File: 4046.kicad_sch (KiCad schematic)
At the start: 10 parts, among them SW2 PLL Type, U2 4046

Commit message: schematic finished
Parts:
- renumbered R6 to R10, R8 to R11, R4 to R8, R5 to R9, SW2 to SW6
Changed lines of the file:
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@@
+					(unit 1)
+				)
+				(path "/01c1f2c1-4d06-4880-847a-9ab55552e3fd/ad1f1d92-237d-4bc3-883c-2ce266dd223f/a3fe2060-ea4c-4d2b-9ba5-3084b7e4dd13"
+					(reference "C4")
 					(unit 1)
 				)
@@
 		(on_board yes)
 		(dnp no)
-		(property "Reference" "SW2"
+		(property "Reference" "SW6"
 			(at 179.07 65.024 0)
 			(effects
@@
 			(project "kleingorium"
 				(path "/01c1f2c1-4d06-4880-847a-9ab55552e3fd/ad1f1d92-237d-4bc3-883c-2ce266dd223f/24602293-d4e4-4f10-aa56-94ee1e111e94"
-					(reference "SW2")
+					(reference "SW6")
+					(unit 1)
+				)
+				(path "/01c1f2c1-4d06-4880-847a-9ab55552e3fd/ad1f1d92-237d-4bc3-883c-2ce266dd223f/a3fe2060-ea4c-4d2b-9ba5-3084b7e4dd13"
+					(reference "SW7")
 					(unit 1)
 				)
@@
 		(dnp no)
 		(fields_autoplaced yes)
-		(property "Reference" "#PWR010"
+		(property "Reference" "#PWR017"
 			(at 152.4 50.8 0)
 			(effects
@@
 			(project "kleingorium"
 				(path "/01c1f2c1-4d06-4880-847a-9ab55552e3fd/ad1f1d92-237d-4bc3-883c-2ce266dd223f/24602293-d4e4-4f10-aa56-94ee1e111e94"
-					(reference "#PWR010")
+					(reference "#PWR017")
+					(unit 1)
+				)
+				(path "/01c1f2c1-4d06-4880-847a-9ab55552e3fd/ad1f1d92-237d-4bc3-883c-2ce266dd223f/a3fe2060-ea4c-4d2b-9ba5-3084b7e4dd13"
+					(reference "#PWR048")
 					(unit 1)
 				)
@@
 					(unit 1)
 				)
+				(path "/01c1f2c1-4d06-4880-847a-9ab55552e3fd/ad1f1d92-237d-4bc3-883c-2ce266dd223f/a3fe2060-ea4c-4d2b-9ba5-3084b7e4dd13"
+					(reference "U8")
+					(unit 1)
+				)
 			)
 		)
@@
 		(dnp no)
 		(fields_autoplaced yes)
-		(property "Reference" "R8"
+		(property "Reference" "R11"
 			(at 184.15 77.4699 0)
 			(effects
@@
 			(project "kleingorium"
 				(path "/01c1f2c1-4d06-4880-847a-9ab55552e3fd/ad1f1d92-237d-4bc3-883c-2ce266dd223f/24602293-d4e4-4f10-aa56-94ee1e111e94"
-					(reference "R8")
+					(reference "R11")
+					(unit 1)
+				)
+				(path "/01c1f2c1-4d06-4880-847a-9ab55552e3fd/ad1f1d92-237d-4bc3-883c-2ce266dd223f/a3fe2060-ea4c-4d2b-9ba5-3084b7e4dd13"
+					(reference "R29")
 					(unit 1)
 				)
@@
 		(dnp no)
 		(fields_autoplaced yes)
-		(property "Reference" "#PWR07"
+		(property "Reference" "#PWR015"
 			(at 128.27 114.3 0)
 			(effects
@@
 			(project "kleingorium"
 				(path "/01c1f2c1-4d06-4880-847a-9ab55552e3fd/ad1f1d92-237d-4bc3-883c-2ce266dd223f/24602293-d4e4-4f10-aa56-94ee1e111e94"
-					(reference "#PWR07")
+					(reference "#PWR015")
+					(unit 1)
+				)
+				(path "/01c1f2c1-4d06-4880-847a-9ab55552e3fd/ad1f1d92-237d-4bc3-883c-2ce266dd223f/a3fe2060-ea4c-4d2b-9ba5-3084b7e4dd13"
+					(reference "#PWR046")
 					(unit 1)
 				)
@@
 		(on_board yes)
 		(dnp no)
-		(property "Reference" "R6"
+		(property "Reference" "R10"
 			(at 192.278 65.532 0)
 			(effects
@@
 			(project "kleingorium"
 				(path "/01c1f2c1-4d06-4880-847a-9ab55552e3fd/ad1f1d92-237d-4bc3-883c-2ce266dd223f/24602293-d4e4-4f10-aa56-94ee1e111e94"
-					(reference "R6")
+					(reference "R10")
+					(unit 1)
+				)
+				(path "/01c1f2c1-4d06-4880-847a-9ab55552e3fd/ad1f1d92-237d-4bc3-883c-2ce266dd223f/a3fe2060-ea4c-4d2b-9ba5-3084b7e4dd13"
+					(reference "R28")
 					(unit 1)
 				)
@@
 		(dnp no)
 		(fields_autoplaced yes)
-		(property "Reference" "#PWR015"
+		(property "Reference" "#PWR019"
 			(at 173.99 115.57 0)
 			(effects
@@
 			(project "kleingorium"
 				(path "/01c1f2c1-4d06-4880-847a-9ab55552e3fd/ad1f1d92-237d-4bc3-883c-2ce266dd223f/24602293-d4e4-4f10-aa56-94ee1e111e94"
-					(reference "#PWR015")
+					(reference "#PWR019")
+					(unit 1)
+				)
+				(path "/01c1f2c1-4d06-4880-847a-9ab55552e3fd/ad1f1d92-237d-4bc3-883c-2ce266dd223f/a3fe2060-ea4c-4d2b-9ba5-3084b7e4dd13"
+					(reference "#PWR050")
 					(unit 1)
 				)
@@
 		(dnp no)
 		(fields_autoplaced yes)
-		(property "Reference" "R4"
+		(property "Reference" "R8"
 			(at 130.81 97.7899 0)
 			(effects
@@
 			(project "kleingorium"
 				(path "/01c1f2c1-4d06-4880-847a-9ab55552e3fd/ad1f1d92-237d-4bc3-883c-2ce266dd223f/24602293-d4e4-4f10-aa56-94ee1e111e94"
-					(reference "R4")
+					(reference "R8")
+					(unit 1)
+				)
+				(path "/01c1f2c1-4d06-4880-847a-9ab55552e3fd/ad1f1d92-237d-4bc3-883c-2ce266dd223f/a3fe2060-ea4c-4d2b-9ba5-3084b7e4dd13"
+					(reference "R26")
 					(unit 1)
 				)
@@
 		(dnp no)
 		(fields_autoplaced yes)
-		(property "Reference" "#PWR014"
+		(property "Reference" "#PWR018"
 			(at 152.4 114.3 0)
 			(effects
@@
 			(project "kleingorium"
 				(path "/01c1f2c1-4d06-4880-847a-9ab55552e3fd/ad1f1d92-237d-4bc3-883c-2ce266dd223f/24602293-d4e4-4f10-aa56-94ee1e111e94"
-					(reference "#PWR014")
+					(reference "#PWR018")
+					(unit 1)
+				)
+				(path "/01c1f2c1-4d06-4880-847a-9ab55552e3fd/ad1f1d92-237d-4bc3-883c-2ce266dd223f/a3fe2060-ea4c-4d2b-9ba5-3084b7e4dd13"
+					(reference "#PWR049")
 					(unit 1)
 				)
@@
 		(dnp no)
 		(fields_autoplaced yes)
-		(property "Reference" "R5"
+		(property "Reference" "R9"
 			(at 142.24 97.7899 0)
 			(effects
@@
 			(project "kleingorium"
 				(path "/01c1f2c1-4d06-4880-847a-9ab55552e3fd/ad1f1d92-237d-4bc3-883c-2ce266dd223f/24602293-d4e4-4f10-aa56-94ee1e111e94"
-					(reference "R5")
+					(reference "R9")
+					(unit 1)
+				)
+				(path "/01c1f2c1-4d06-4880-847a-9ab55552e3fd/ad1f1d92-237d-4bc3-883c-2ce266dd223f/a3fe2060-ea4c-4d2b-9ba5-3084b7e4dd13"
+					(reference "R27")
 					(unit 1)
 				)
@@
 		(on_board yes)
 		(dnp no)
-		(property "Reference" "#PWR06"
+		(property "Reference" "#PWR014"
 			(at 116.84 87.63 0)
 			(effects
@@
 			(project "kleingorium"
 				(path "/01c1f2c1-4d06-4880-847a-9ab55552e3fd/ad1f1d92-237d-4bc3-883c-2ce266dd223f/24602293-d4e4-4f10-aa56-94ee1e111e94"
-					(reference "#PWR06")
+					(reference "#PWR014")
+					(unit 1)
+				)
+				(path "/01c1f2c1-4d06-4880-847a-9ab55552e3fd/ad1f1d92-237d-4bc3-883c-2ce266dd223f/a3fe2060-ea4c-4d2b-9ba5-3084b7e4dd13"
+					(reference "#PWR045")
 					(unit 1)
 				)
@@
 					(unit 1)
 				)
+				(path "/01c1f2c1-4d06-4880-847a-9ab55552e3fd/ad1f1d92-237d-4bc3-883c-2ce266dd223f/a3fe2060-ea4c-4d2b-9ba5-3084b7e4dd13"
+					(reference "C6")
+					(unit 1)
+				)
 			)
 		)
@@
 		(dnp no)
 		(fields_autoplaced yes)
-		(property "Reference" "#PWR09"
+		(property "Reference" "#PWR016"
 			(at 139.7 114.3 0)
 			(effects
@@
 			(project "kleingorium"
 				(path "/01c1f2c1-4d06-4880-847a-9ab55552e3fd/ad1f1d92-237d-4bc3-883c-2ce266dd223f/24602293-d4e4-4f10-aa56-94ee1e111e94"
-					(reference "#PWR09")
+					(reference "#PWR016")
+					(unit 1)
+				)
+				(path "/01c1f2c1-4d06-4880-847a-9ab55552e3fd/ad1f1d92-237d-4bc3-883c-2ce266dd223f/a3fe2060-ea4c-4d2b-9ba5-3084b7e4dd13"
+					(reference "#PWR047")
 					(unit 1)
 				)
@@
 					(unit 1)
 				)
+				(path "/01c1f2c1-4d06-4880-847a-9ab55552e3fd/ad1f1d92-237d-4bc3-883c-2ce266dd223f/a3fe2060-ea4c-4d2b-9ba5-3084b7e4dd13"
+					(reference "C5")
+					(unit 1)
+				)
 			)
 		)
@@
 					(unit 1)
 				)
+				(path "/01c1f2c1-4d06-4880-847a-9ab55552e3fd/ad1f1d92-237d-4bc3-883c-2ce266dd223f/a3fe2060-ea4c-4d2b-9ba5-3084b7e4dd13"
+					(reference "RV2")
+					(unit 1)
+				)

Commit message: wip symmetric layout
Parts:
- renumbered C1 to C4, C2 to C5, C3 to C6, R8 to R27, R9 to R28, R10 to R29, R11 to R30, RV1 to RV2, U2 to U9

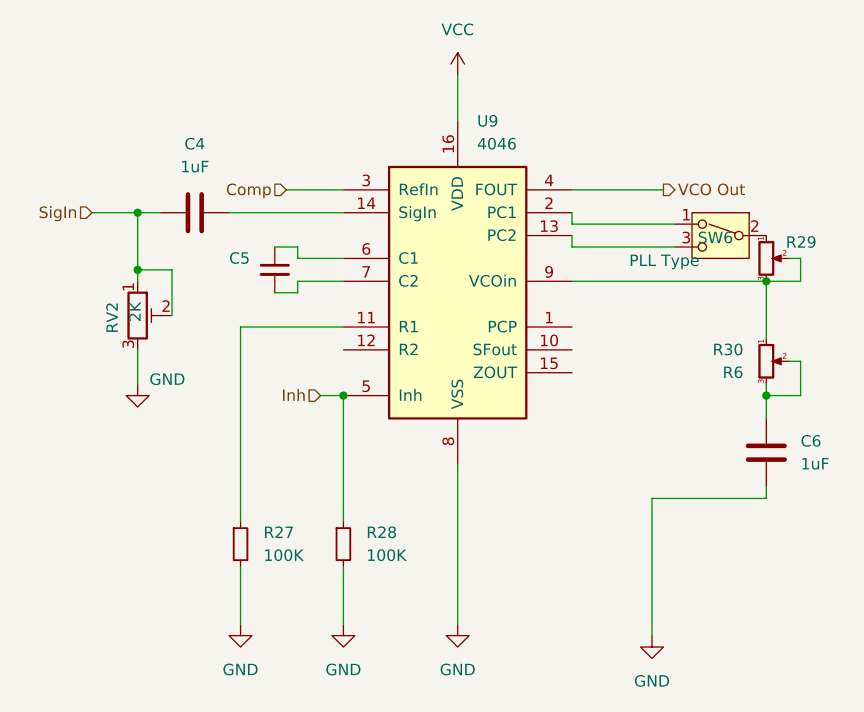
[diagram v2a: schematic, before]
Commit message: two halves routing
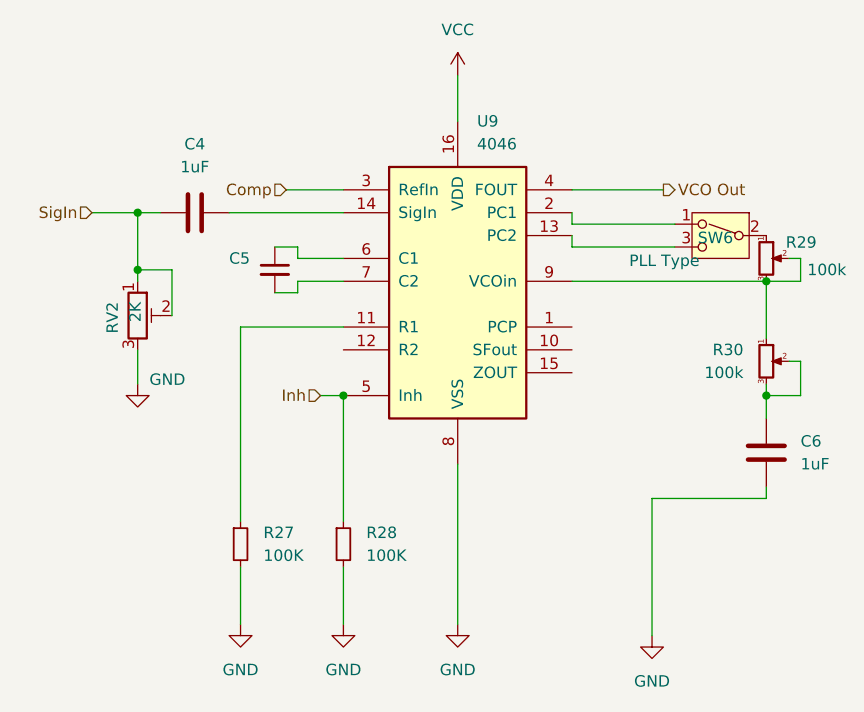
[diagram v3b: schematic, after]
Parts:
- R29: value R5 -> 100k
- R30: value R6 -> 100k
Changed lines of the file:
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@@
 			)
 		)
-		(property "Value" "R6"
+		(property "Value" "100k"
 			(at 184.15 80.0099 0)
 			(effects
@@
 			)
 		)
-		(property "Value" "R5"
-			(at 184.15 68.5799 0)
+		(property "Value" "100k"
+			(at 195.58 68.58 0)
 			(effects
 				(font
@@
 				)
 				(justify right)
-				(hide yes)
 			)
 		)
